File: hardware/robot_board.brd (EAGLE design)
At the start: 95.2 x 76.1 mm, 135 parts, among them J1 POWER_JACKPTH, Q1 DMP2035U, Q2 DMP2035U, Q3 DMP2035U-7, Q4 DMP2035U-7, U1 FT232RL-BASICSSOP, U11 LM393, U12 LM393, U16 LM393, U17 ATMEGA325PA, U2 SIA907EDJT, U3 MIC5219, U5 SIA907EDJT, U6 SIA907EDJT, U7 TLV70233, Y1 16MHz

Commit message: more routing
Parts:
- moved JP7 71.9 mm to (9.40, 74.4)
- moved JP6 66.8 mm to (9.40, 71.9)
- moved JP10 65.2 mm to (53.3, 71.4), turned to 0 degrees
- moved U$19 64.5 mm to (32.8, 69.3), turned to 180 degrees
- moved U$20 64.5 mm to (21.6, 69.3), turned to 180 degrees
- moved C3 63.9 mm to (39.1, 4.83), turned to 0 degrees
- moved IR 63.4 mm to (3.81, 10.4), turned to 90 degrees
- moved C5 63.1 mm to (4.83, 49.0), turned to 180 degrees
- moved JP3 61.7 mm to (9.40, 69.3)
- moved R47 54.6 mm to (9.40, 64.5), turned to 90 degrees
- moved JP8 53.7 mm to (64.8, 63.5), turned to 0 degrees
- moved R50 53.4 mm to (17.0, 64.5), turned to 90 degrees
- moved U$4 52.4 mm to (29.5, 63.8), turned to 180 degrees
- moved U$5 52.3 mm to (23.9, 63.8), turned to 180 degrees
- moved R48 51.9 mm to (11.9, 64.5), turned to 90 degrees
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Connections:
- net 5V: no longer JP6.1, JP6.2, JP6.3, JP6.4
- net VIN_F: now also JP6.1, JP6.2, JP6.3, JP6.4
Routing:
- net VIN_F: track 77.0 -> 206.8 mm
- net GND: track 293.7 -> 408.7 mm, vias 17 -> 33
- net 5V_UC: track 0.00 -> 109.7 mm, vias 0 -> 6
- net A4_IN: track 5.08 -> 105.2 mm, vias 0 -> 6
- net A5_IN: track 3.94 -> 95.4 mm, vias 0 -> 4
- net SDA_IN: track 0.00 -> 90.4 mm, vias 0 -> 8
- net A3_IN: track 4.36 -> 93.8 mm, vias 0 -> 6
- net A2_IN: track 3.44 -> 90.3 mm, vias 0 -> 6
- net A1_IN: track 3.02 -> 81.2 mm, vias 0 -> 4
- net A0_IN: track 3.02 -> 78.3 mm, vias 0 -> 4
- net SCL_IN: track 4.35 -> 75.6 mm, vias 0 -> 8
- net D6_IN: track 2.62 -> 65.3 mm, vias 0 -> 4
- net TX: track 0.00 -> 61.7 mm, vias 0 -> 4
- net RX: track 0.00 -> 58.7 mm, vias 0 -> 2
- net D13: track 5.13 -> 62.2 mm, vias 0 -> 3
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- added copper zone on layer 16, net GND

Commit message: more routing
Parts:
- moved C3 54.7 mm to (61.7, 54.6), turned to 270 degrees
- moved IR 1.52 mm to (3.81, 8.89)
- moved C2 1.27 mm to (7.87, 15.5), turned to 180 degrees
- moved R28 1.05 mm to (58.7, 40.1)
- moved D30 0.76 mm to (2.54, 29.7)
- moved R40 0.76 mm to (2.54, 41.7)
- moved R51 0.76 mm to (2.54, 35.3)
- moved R52 0.76 mm to (2.54, 18.3)
- moved U11 0.76 mm to (62.5, 40.1)
- moved R33 0.76 mm to (67.6, 40.4)
- moved D31 0.51 mm to (2.54, 23.6)
- moved R55 0.25 mm to (28.7, 9.65)
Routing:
- net 5V: track 87.7 -> 229.0 mm, vias 7 -> 17
- net RESET: track 82.8 -> 200.1 mm, vias 6 -> 12
- net M1_DIR1: track 0.00 -> 79.6 mm, vias 0 -> 4
- net 3V3: track 63.1 -> 141.0 mm, vias 6 -> 8
- net ACCEL_INT: track 0.00 -> 54.7 mm, vias 0 -> 6
- net M1_DIR0: track 0.00 -> 54.6 mm, vias 0 -> 4
- net N$52: track 5.18 -> 56.2 mm, vias 0 -> 4
- net GND: track 408.7 -> 390.8 mm, vias 33 -> 36
- net DTR: track 0.00 -> 8.78 mm, vias 0 -> 2
- net M0_EN: track 34.9 -> 43.0 mm, vias 2 -> 4
- net USBGATE: track 28.1 -> 32.2 mm
- net SDA_IN: track 90.4 -> 93.4 mm, vias 8 -> 10
- net TX: track 61.7 -> 58.8 mm
- net A3_IN: track 93.8 -> 96.5 mm
- net N$3: track 29.9 -> 32.5 mm
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
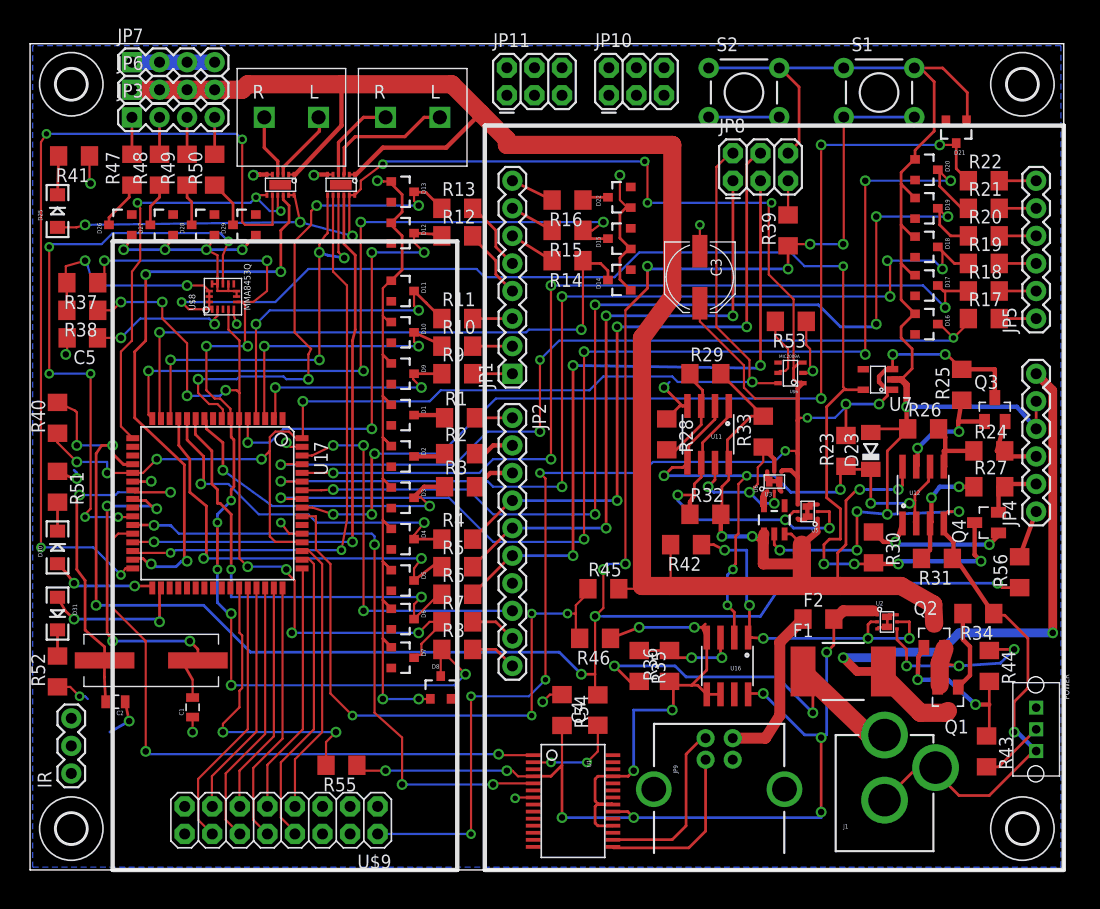
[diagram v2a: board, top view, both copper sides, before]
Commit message: added Bluetooth module
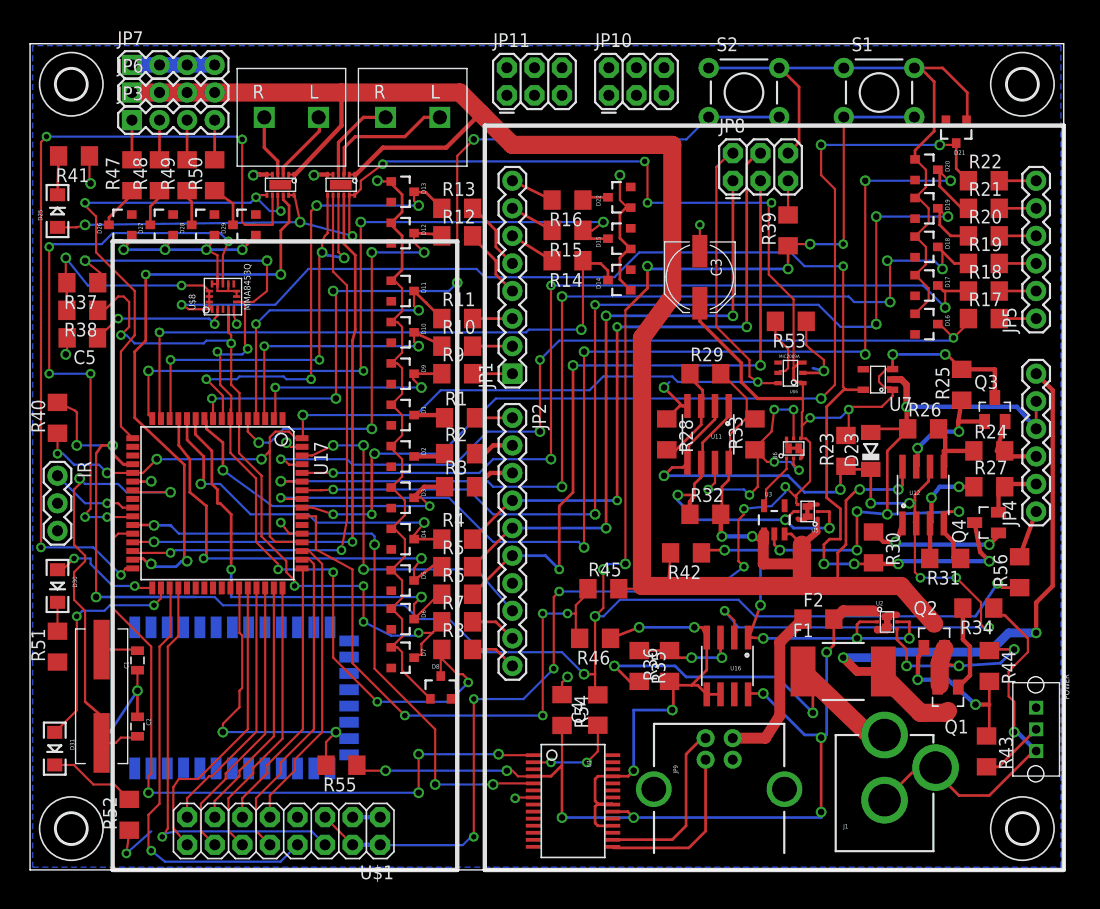
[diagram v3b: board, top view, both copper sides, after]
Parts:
- removed U$9: M08X2, SparkFun-Connectors:2X8
- added U$1: M08X2, SparkFun-Connectors:2X8
- added U4: HC_05, SerialPortBluetooth:BLUETOOTH_SMD
- D1, D10, D11, D12, D13, D14, D15, D16, D17, D18, D19, D2, D20, D21, D22, D26, D27, D28, D29, D3, D4, D5, D6, D7, D8, D9: value (none) -> 5.1V
- moved IR 27.5 mm to (2.54, 36.3), turned to 270 degrees
- moved R52 14.8 mm to (9.14, 5.08)
- moved R51 14.7 mm to (2.54, 20.6), turned to 90 degrees
- moved D31 12.4 mm to (2.29, 11.2)
- moved C1 6.67 mm to (9.91, 19.3)
- moved Y1 5.64 mm to (6.60, 16.0), turned to 270 degrees
- moved D30 3.56 mm to (2.54, 26.2), turned to 270 degrees
- moved U6 3.53 mm to (70.4, 38.9)
- moved C2 3.06 mm to (9.91, 13.2), turned to 270 degrees
- moved R33 0.80 mm to (66.8, 40.1)
- moved R31 0.76 mm to (84.3, 28.7)
- moved R42 0.76 mm to (60.5, 29.2)
- moved R47 0.51 mm to (9.40, 64.0)
- moved R48 0.51 mm to (11.9, 64.0)
- moved R49 0.51 mm to (14.5, 64.0)
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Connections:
- removed net LCD_E: U17.19
- removed net LCD_RS: U17.18
- removed net N$47: U$9.3
- removed net N$48: U$9.5
- removed net N$59: U$9.6
- removed net N$60: U$9.4
- new net E: U$1.8, U17.35
- new net IR: IR.1, U17.25
- new net RS: U$1.6, U17.36
- net 5V: now also IR.2, U$1.2, U$1.4, U$1.5; no longer U$9.2
- net GND: now also IR.3, U$1.1, U$1.3, U$1.7; no longer U$9.1
- net LCD0: now also U$1.9; no longer U$9.7
- net LCD1: now also U$1.10; no longer U$9.8
- net LCD2: now also U$1.11; no longer U$9.9
- net LCD3: now also U$1.12; no longer U$9.10
- net LCD4: now also U$1.13; no longer U$9.11
- net LCD5: now also U$1.14; no longer U$9.12
- net LCD6: now also U$1.15; no longer U$9.13
- net LCD7: now also U$1.16; no longer U$9.14
- net SW1: now also U17.9
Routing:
- net SW1: track 6.50 -> 77.9 mm, vias 0 -> 5
- net E: track 0.00 -> 39.7 mm, vias 0 -> 1
- net RS: track 0.00 -> 39.3 mm, vias 0 -> 1
- net N$4: track 34.3 -> 3.34 mm, vias 4 -> 0
- net 2.1V: track 59.8 -> 87.1 mm, vias 7 -> 8
- net GND: track 390.8 -> 370.5 mm, vias 36 -> 32
- net N$3: track 32.5 -> 42.8 mm
- net IR: track 0.00 -> 8.15 mm, vias 0 -> 1
- net 5VREG_SW: track 18.9 -> 27.0 mm, vias 3 -> 6
- net RX: track 58.7 -> 66.1 mm, vias 2 -> 4
- net LED1: track 13.7 -> 20.9 mm
- net M1_EN: track 39.6 -> 46.0 mm
- net N$62: track 2.41 -> 8.17 mm
- net SCL_IN: track 74.2 -> 68.9 mm, vias 8 -> 6
- net VIN_F: track 209.1 -> 205.1 mm
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
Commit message: reversed digital/analog pins
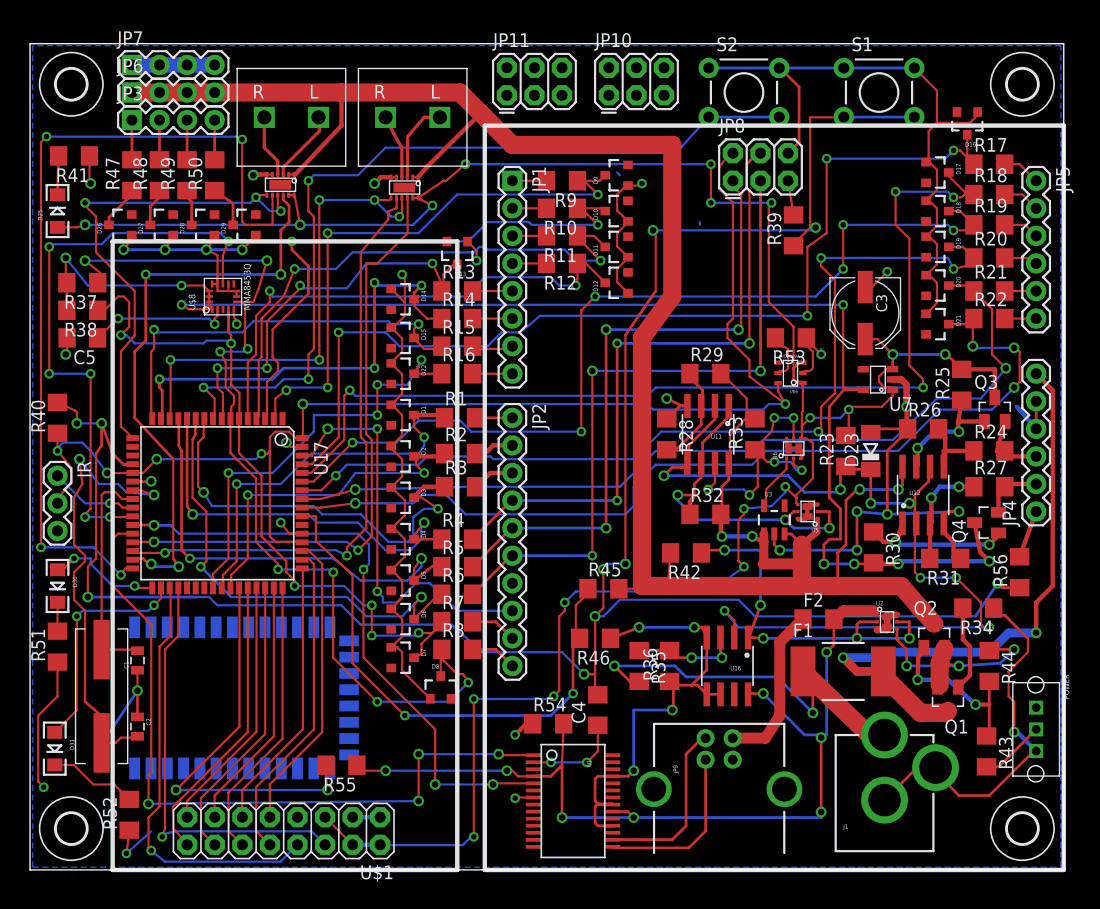
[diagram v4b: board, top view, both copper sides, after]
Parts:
- moved D9 27.0 mm to (54.1, 64.0), turned to 90 degrees
- moved D22 25.8 mm to (34.3, 45.7), turned to 270 degrees
- moved D10 22.7 mm to (54.1, 60.7), turned to 90 degrees
- moved D15 22.1 mm to (34.3, 49.0), turned to 270 degrees
- moved D12 20.3 mm to (54.1, 54.1), turned to 90 degrees
- moved R9 20.2 mm to (49.0, 63.5), turned to 180 degrees
- moved D11 20.2 mm to (54.1, 57.4), turned to 90 degrees
- moved D14 20.1 mm to (34.3, 52.6), turned to 270 degrees
- moved R16 19.0 mm to (39.4, 45.7), turned to 0 degrees
- moved D16 18.9 mm to (86.4, 68.8), turned to 180 degrees
- moved D21 17.9 mm to (83.6, 50.3), turned to 270 degrees
- moved JP1 17.8 mm to (44.5, 63.5), turned to 270 degrees
- moved R10 16.0 mm to (49.0, 61.0), turned to 180 degrees
- moved C3 15.6 mm to (77.0, 51.3)
- moved R15 14.7 mm to (39.4, 48.3), turned to 0 degrees
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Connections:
- net 5V: no longer IR.2
- net 5V_UC: now also IR.2
- net D7_IN: now also U17.40
- net D8_IN: now also U17.41
- net D9_IN: now also U17.42
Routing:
- net D7_IN: track 2.41 -> 40.2 mm, vias 0 -> 4
- net D0_IN: track 20.6 -> 53.0 mm, vias 2 -> 4
- net D8_IN: track 3.07 -> 35.2 mm, vias 0 -> 2
- net D9_IN: track 3.07 -> 31.6 mm, vias 0 -> 2
- net D1_IN: track 25.3 -> 53.4 mm
- net D6_IN: track 65.3 -> 37.9 mm, vias 4 -> 2
- net A4_IN: track 106.4 -> 80.4 mm, vias 6 -> 2
- net D2_IN: track 29.8 -> 50.7 mm
- net N$4: track 3.34 -> 20.8 mm
- net D5_IN: track 56.9 -> 42.1 mm, vias 2 -> 4
- net A0_IN: track 77.4 -> 90.8 mm
- net GND: track 370.5 -> 357.9 mm, vias 32 -> 34
- net 5V_UC: track 110.0 -> 122.5 mm
- net 5V: track 229.5 -> 217.6 mm
- net A3_IN: track 96.5 -> 84.9 mm, vias 6 -> 4
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
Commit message: updated bluetooth
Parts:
- added C6: .1uF, resistor:C1206
- added C7: 22uF, resistor:C1206
- added D24: POWER, SparkFun-LED:LED-1206
- added D32: 5.1V, SparkFun-DiscreteSemi:SOT23-3
- added D33: BAT54C, diode:SOT23
- added R57: 330, resistor:R1206
- added R58, R60: 300K, resistor:R1206
- added R59, R61: 1K, resistor:R1206
- added R62: 2K, resistor:R1206
- R23, R27, R28, R35, R45, R46: value (none) -> 10K
- R24: value (none) -> 12K
- R26: value (none) -> 7.68K
- R29, R31: value (none) -> 15K
- R36: value (none) -> 20K
- moved U2 12.6 mm to (67.1, 18.8), turned to 0 degrees
- moved F2 9.45 mm to (67.1, 15.5), turned to 180 degrees
- moved R42 6.59 mm to (63.5, 23.4), turned to 0 degrees
- moved R35 4.34 mm to (54.6, 14.7)
- moved R36 3.06 mm to (56.9, 16.5)
- moved U16 2.65 mm to (61.7, 18.0)
- moved R55 2.34 mm to (30.5, 11.2)
- moved R56 1.27 mm to (91.9, 28.4)
- moved R25 1.02 mm to (84.8, 44.7)
- moved C2 0.80 mm to (10.2, 14.0)
- moved Q3 0.76 mm to (88.1, 42.4)
- moved R43 0.57 mm to (87.6, 11.2)
- moved C1 0.57 mm to (10.2, 18.8)
- moved R52 0.51 mm to (9.14, 4.57)
- moved D30 0.25 mm to (2.29, 26.2)
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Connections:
- removed net N$31: U$6.P$4
- new net AREF_IN: D32.3, R59.1, U17.62
- new net N$10: D24.A, U1.22
- new net N$11: D24.C, R57.2
- new net N$12: D33.3, R42.2
- new net N$14: R61.2, U4.1
- net 3V3: now also C7.1, U4.12; no longer R30.2
- net 3V3_OUT: now also R30.2
- net 5V: now also C6.1; no longer R25.2
- net 5VREG_SWO: now also R58.1
- net 5V_OUT: now also JP10.3, JP10.4, JP11.3, JP11.4, R25.2
- net A0: now also JP10.1
- net A1: now also JP10.2
- net AREF: now also R59.2; no longer U17.62
- net D0: now also JP11.1
- net D0_IN: now also R61.1, R62.2
- net D1: now also JP11.2
- net D1_IN: now also U4.2
- net GND: now also C6.2, C7.2, D32.1, JP10.5, JP10.6, JP11.5, JP11.6, R57.1, R60.1, R62.1, U4.13, U4.22
- net N$35: now also R58.2
- net PWR_SW: now also D33.1
- net USBGATE: now also R60.2
- net USB_5V: now also D33.2
- net VIN_F: no longer R42.2
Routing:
- net 3V3: track 135.0 -> 243.7 mm, vias 8 -> 10
- net D1_IN: track 53.4 -> 149.7 mm, vias 2 -> 8
- net 5V_OUT: track 6.95 -> 94.0 mm, vias 0 -> 5
- net A1: track 3.42 -> 56.0 mm, vias 0 -> 1
- net A0: track 3.53 -> 45.5 mm, vias 0 -> 2
- net AREF_IN: track 0.00 -> 40.7 mm, vias 0 -> 4
- net GND: track 357.9 -> 319.7 mm, vias 34 -> 30
- net D0_IN: track 53.0 -> 90.3 mm, vias 4 -> 8
- net AREF: track 38.4 -> 3.91 mm, vias 3 -> 0
- net 3V3_OUT: track 6.08 -> 26.5 mm, vias 0 -> 2
- net D1: track 3.15 -> 18.7 mm, vias 0 -> 2
- net N$10: track 0.00 -> 15.3 mm, vias 0 -> 2
- net PWR_SW: track 22.1 -> 34.9 mm
- net USB_5V: track 86.4 -> 98.3 mm, vias 8 -> 9
- net USBGATE: track 34.6 -> 23.3 mm, vias 5 -> 3
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
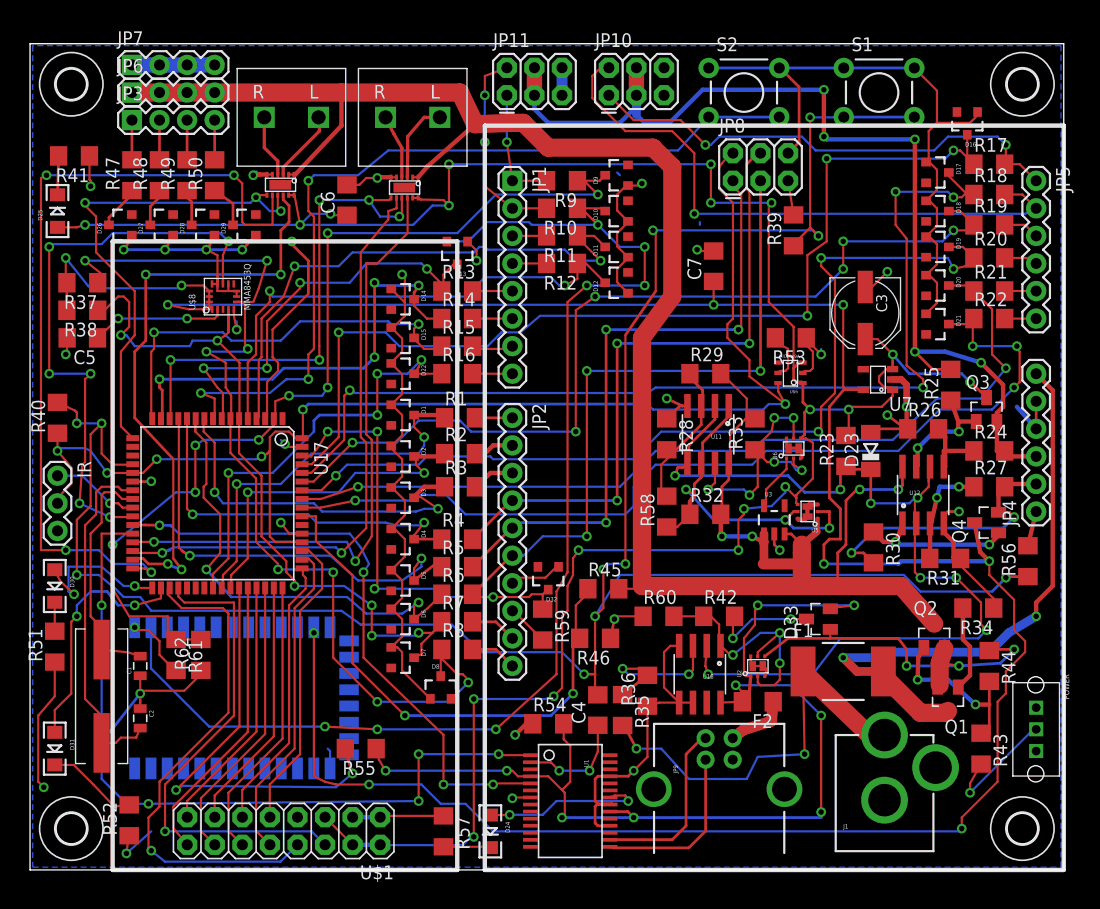
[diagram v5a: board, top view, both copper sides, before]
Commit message: updated Bluetooth pinout
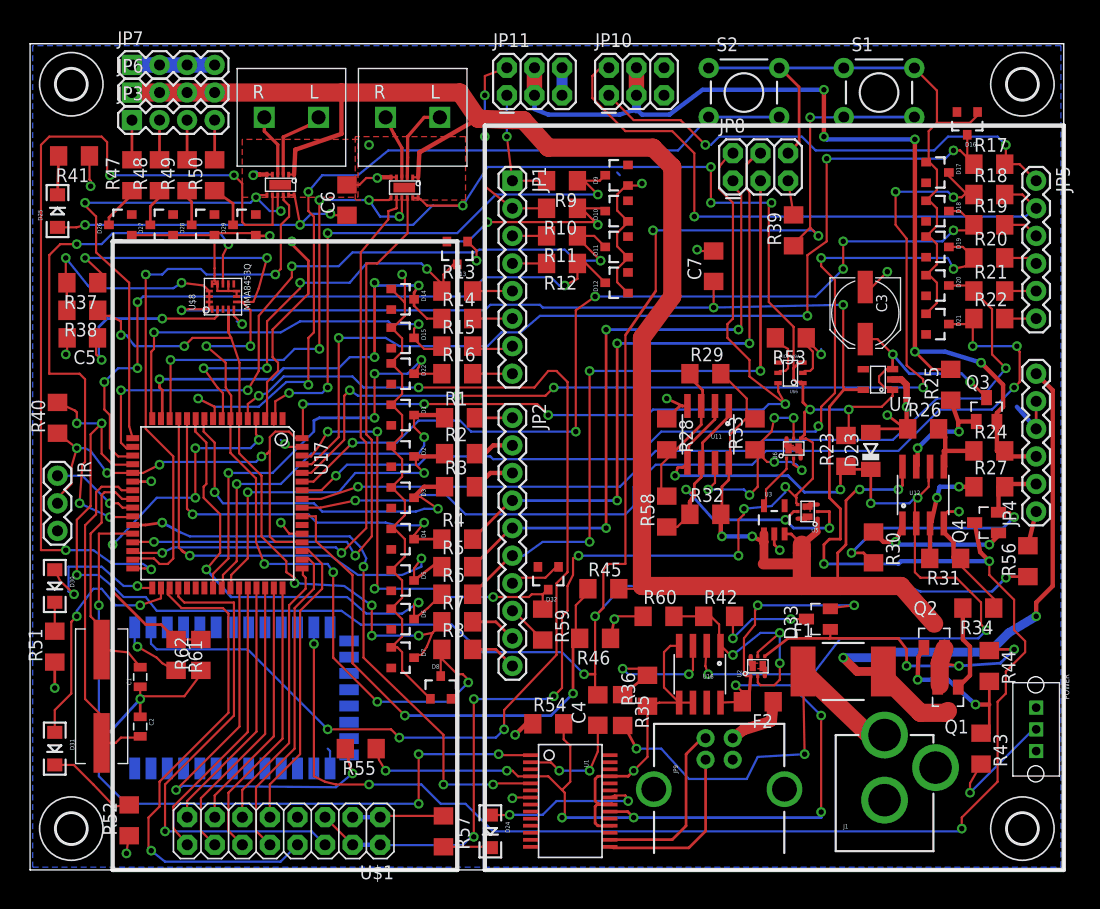
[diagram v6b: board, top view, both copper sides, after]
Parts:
- moved C1 1.02 mm to (10.2, 17.8)
- moved C2 0.76 mm to (10.2, 13.2)
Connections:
- new net BT_RX: U17.5, U4.2
- new net BT_TX: R61.1, R62.2, U17.4
- net 5V: now also U5.S2, U6.S2; no longer U5.P$3, U6.P$3
- net 5VREG_SW: now also U6.G1, U6.G2; no longer U6.P$2, U6.P$5
- net 5VREG_SWO: now also U5.G1, U5.G2; no longer U5.P$2, U5.P$5
- net D0_IN: no longer R61.1, R62.2
- net D1_IN: no longer U4.2
- net D2_IN: now also U17.18; no longer U17.4
- net D3_IN: now also U17.19; no longer U17.5
- net GND: now also U$4.GND, U$5.GND, U4.34
- net HIGH_5V_REG: now also U6.S1; no longer U6.P$6
- net N$28: now also U2.D1, U2.D1@, U2.D2, U2.D2@; no longer U2.P$1, U2.P$4
- net N$42: now also U6.D1, U6.D1@, U6.D2, U6.D2@; no longer U6.P$1, U6.P$4
- net N$44: now also U5.D1, U5.D1@, U5.D2, U5.D2@; no longer U5.P$1, U5.P$4
- net PWR_SW: now also U2.S2; no longer U2.P$3
- net USBGATE: now also U2.G1, U2.G2; no longer U2.P$2, U2.P$5
- net USB_5V: now also U2.S1; no longer U2.P$6
- net VIN_F: now also U5.S1; no longer U5.P$6
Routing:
- net BT_RX: track 0.00 -> 105.6 mm, vias 0 -> 5
- net D1_IN: track 149.7 -> 52.9 mm, vias 8 -> 3
- net D0_IN: track 90.3 -> 53.2 mm, vias 8 -> 4
- net BT_TX: track 0.00 -> 36.6 mm, vias 0 -> 4
- net GND: track 319.7 -> 301.4 mm, vias 30 -> 28
- net D3_IN: track 47.2 -> 65.1 mm, vias 2 -> 4
- net D2_IN: track 50.9 -> 66.3 mm, vias 2 -> 4
- net M1_DIR1: track 75.2 -> 81.3 mm
- net N$8: track 12.5 -> 17.4 mm
- net M1_DIR0: track 54.9 -> 51.8 mm, vias 4 -> 2
- net SCL_IN: track 68.6 -> 65.6 mm
- net VIN_F: track 195.0 -> 197.2 mm
- net 5V_OUT: track 94.0 -> 91.9 mm
- net 3V3: track 243.7 -> 241.7 mm
- net ACCEL_INT: track 54.3 -> 52.8 mm, vias 6 -> 4
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- added copper zone on layer 1, net GND
- added copper zone on layer 1, net N$28
- added copper zone on layer 1, net N$42
- added copper zone on layer 1, net N$44
